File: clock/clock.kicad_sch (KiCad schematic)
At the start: 15 parts, among them Y1 Crystal_16MHz

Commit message: ch
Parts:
- removed C1, C2: C_0805_0.1uf, symbol Device:C
- removed C3, C4: C_0805_22pf, symbol Device:C
- removed D?: LED_0805, symbol Device:D
- removed J?: Conn_01x06, symbol Connector_Generic:Conn_01x06
- removed R1: R_0805_10k, symbol Device:R
- removed R?: R_0805_2.2k, symbol Device:R
- removed SW?: SW_SPST, symbol Switch:SW_SPST
- removed U?: ATmega328-P, Package_DIP:DIP-28_W7.62mm, symbol MCU_Microchip_ATmega:ATmega328-P
- removed Y1: Crystal_16MHz, symbol Device:Crystal
- added C1, C2, C5: C_0805_0.1uf, footprints:C_0805_2012Metric, symbol HPS:C_0805_0.1uf
- added C3, C4: C_0805_22pf, footprints:C_0805_2012Metric, symbol HPS:C_0805_22pf
- added D1: LED_0805, footprints:LED_0805_2012Metric, symbol HPS:LED_0805
- added J1: Conn_01x06, footprints:PinHeader_1x06_P2.54mm_Vertical, symbol HPS:Conn_01x06
- added R1: R_0805_10K, footprints:R_0805_2012Metric, symbol HPS:R_0805_10K
- added R2, R3: R_0805_47, footprints:R_0805_2012Metric, symbol HPS:R_0805_47
- added R4: R_0805_2.2K, footprints:R_0805_2012Metric, symbol HPS:R_0805_2.2K
- added SW1: Omron_B3F_SPST, footprints:SW_SPST_Omron_B3FS-100xP, symbol HPS:Omron_B3F_SPST
- added U1: ATmega328-PU, footprints:DIP-28_W7.62mm, symbol HPS:ATmega328-PU
- added Y1: Crystal_16MHz, footprints:Crystal_SMD_HC49-SD, symbol HPS:Crystal_16MHz
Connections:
- net GND: now also C1.2, C2.2, C3.2, C4.2, J1.5 (Pin_5), J1.6 (Pin_6), R4.2, SW1.1 (A), SW1.2 (A), U1.22 (GND), U1.8 (GND)
- net LED_SCK: now also D1.2 (A), U1.19 (PB5)
- net RESET: now also C5.1, R1.2, SW1.3 (B), SW1.4 (B), U1.1 (~{RESET}/PC6)
- net RXD: now also R3.2, U1.2 (PD0)
- net TXD: now also R2.2, U1.3 (PD1)
- net VCC: now also C2.1, R1.1, U1.20 (AVCC), U1.7 (VCC)
- new net: D1.1 (K), R4.1
- new net: J1.2 (Pin_2), R2.1
- new net: C3.1, U1.10 (XTAL2/PB7), Y1.1
- new net: C1.1, U1.21 (AREF)
- new net: C4.1, U1.9 (XTAL1/PB6), Y1.2
- new net: C5.2, J1.1 (Pin_1)
- new net: J1.3 (Pin_3), R3.1
- no-connect marks 0 -> 1

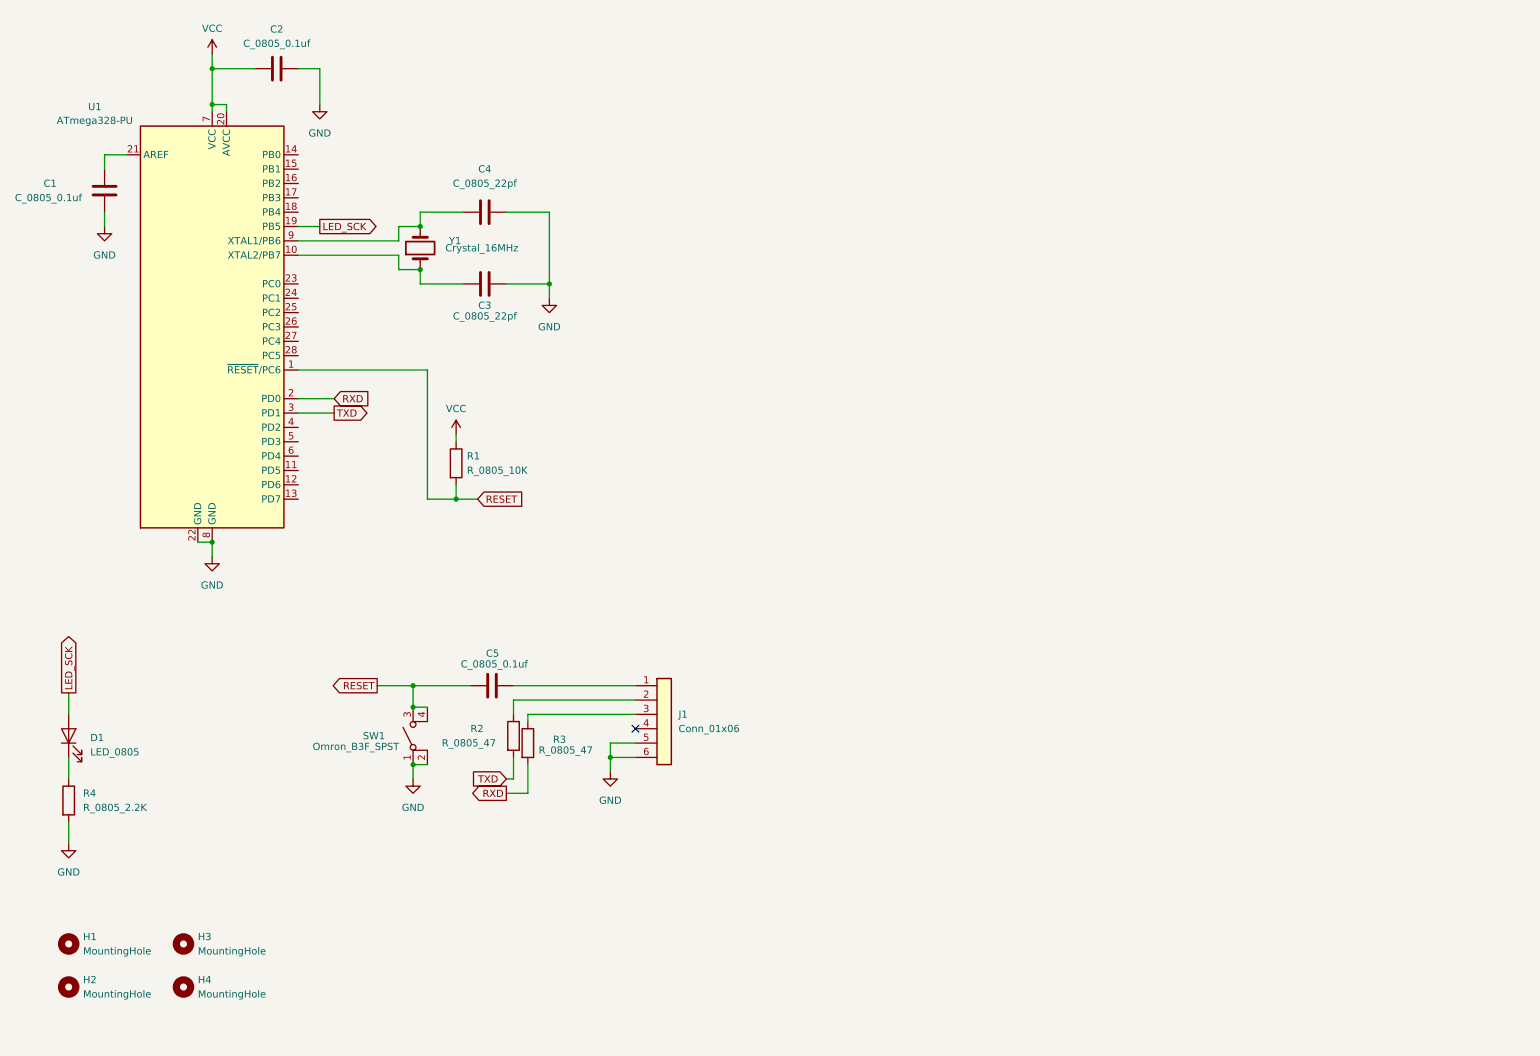
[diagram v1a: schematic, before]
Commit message: appending the clock
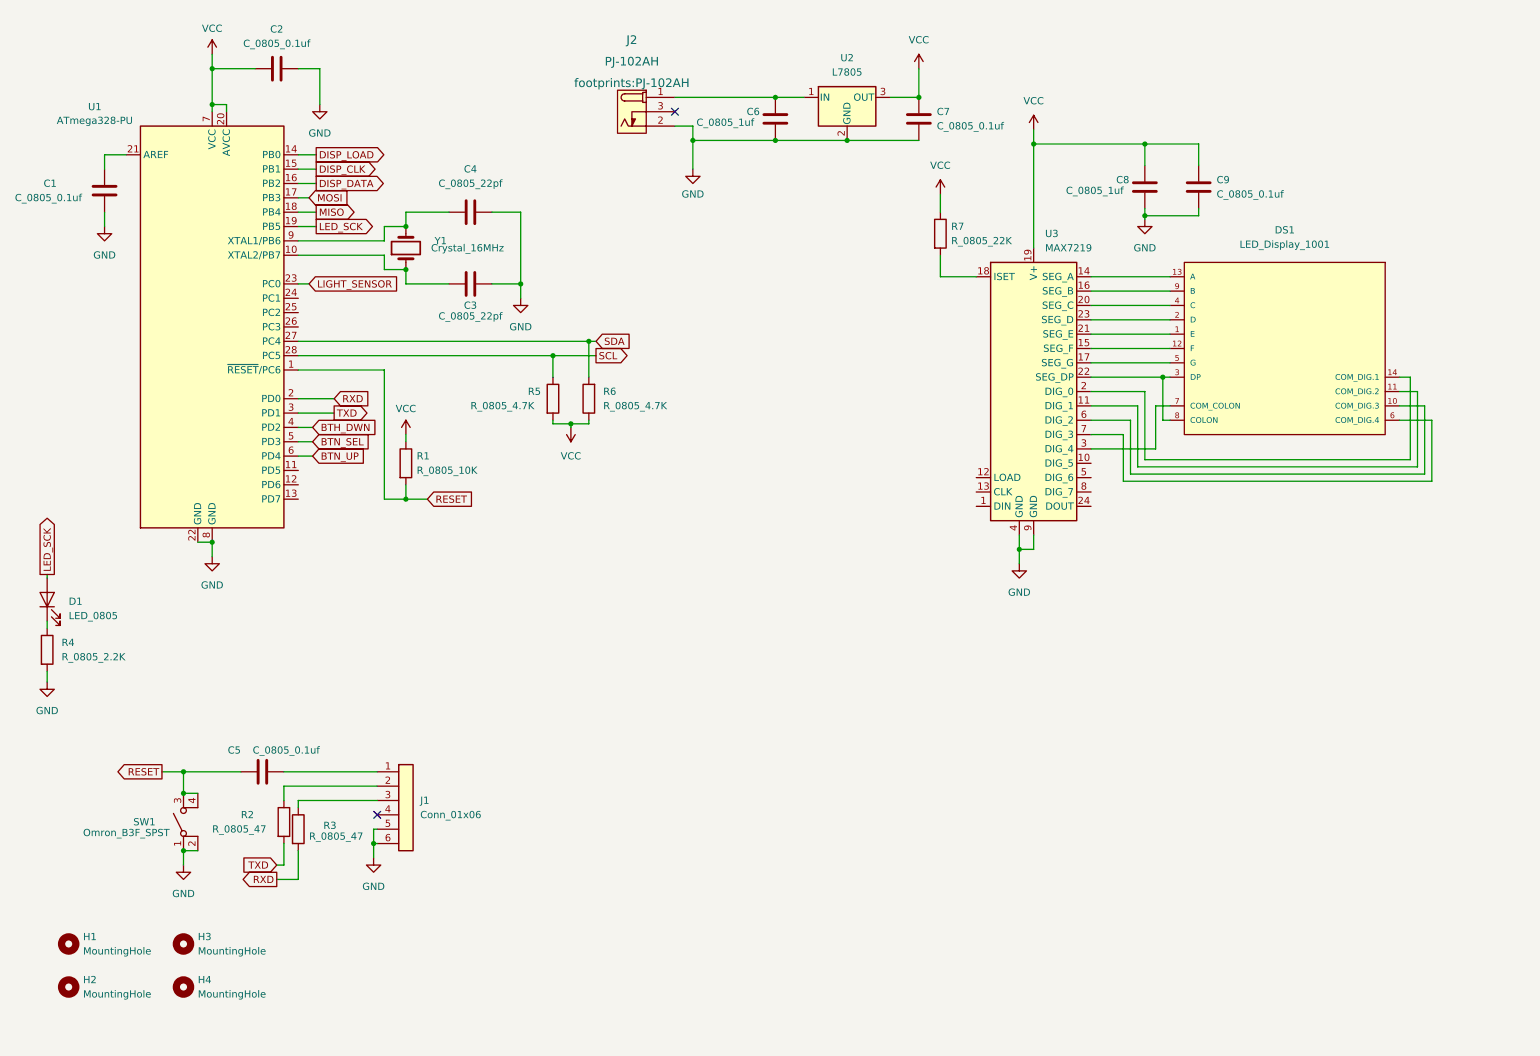
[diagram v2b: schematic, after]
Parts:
- added C6, C8: C_0805_1uf, footprints:C_0805_2012Metric, symbol HPS:C_0805_1uf
- added C7, C9: C_0805_0.1uf, footprints:C_0805_2012Metric, symbol HPS:C_0805_0.1uf
- added DS1: LED_Display_1001, footprints:Adafruit-1001-0-0-MFG, symbol HPS:LED_Display_1001
- added J2: PJ-102AH, footprints:PJ-102AH, symbol HPS:PJ-102AH
- added R5, R6: R_0805_4.7K, footprints:R_0805_2012Metric, symbol HPS:R_0805_4.7K
- added R7: R_0805_22K, footprints:R_0805_2012Metric, symbol HPS:R_0805_22K
- added U2: L7805, symbol HPS:L7805
- added U3: MAX7219, footprints:DIP-24_W7.62mm, symbol HPS:MAX7219
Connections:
- net GND: now also C6.2, C7.2, C8.2, C9.2, J2.2 (OUT), U2.2 (GND), U3.4 (GND), U3.9 (GND)
- net VCC: now also C7.1, C8.1, C9.1, R5.2, R6.1, R7.1, U2.3 (OUT), U3.19 (V+)
- net DISP_LOAD: now reaches U1.14 (PB0)
- net DISP_CLK: now reaches U1.15 (PB1)
- net DISP_DATA: now reaches U1.16 (PB2)
- net MOSI: now reaches U1.17 (PB3)
- net MISO: now reaches U1.18 (PB4)
- net LIGHT_SENSOR: now reaches U1.23 (PC0)
- net SDA: now reaches U1.27 (PC4)
- net SDA: now also R6.2
- net SCL: now reaches U1.28 (PC5)
- net SCL: now also R5.1
- net BTH_DWN: now reaches U1.4 (PD2)
- net BTN_SEL: now reaches U1.5 (PD3)
- net BTN_UP: now reaches U1.6 (PD4)
- new net: DS1.11 (COM_DIG.2), U3.11 (DIG_1)
- new net: DS1.13 (A), U3.14 (SEG_A)
- new net: DS1.12 (F), U3.15 (SEG_F)
- new net: DS1.9 (B), U3.16 (SEG_B)
- new net: DS1.5 (G), U3.17 (SEG_G)
- new net: R7.2, U3.18 (ISET)
- new net: DS1.14 (COM_DIG.1), U3.2 (DIG_0)
- new net: DS1.4 (C), U3.20 (SEG_C)
- new net: DS1.1 (E), U3.21 (SEG_E)
- new net: DS1.3 (DP), DS1.8 (COLON), U3.22 (SEG_DP)
- new net: DS1.2 (D), U3.23 (SEG_D)
- new net: DS1.7 (COM_COLON), U3.3 (DIG_4)
- new net: DS1.10 (COM_DIG.3), U3.6 (DIG_2)
- new net: DS1.6 (COM_DIG.4), U3.7 (DIG_3)
- new net: C6.1, J2.1 (POLE), U2.1 (IN)
- no-connect marks 1 -> 2
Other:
- moved on the sheet: C3, C4, C5, D1, J1, R1, R2, R3, R4, SW1, Y1

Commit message: pre review schematic
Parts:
- added BT1: Battery_Cell, footprints:BatteryHolder_Keystone_106_1x20mm, symbol HPS:Battery_Cell
- added J3: Conn_02x03_Odd_Even, footprints:PinHeader_2x03_P2.54mm_Vertical, symbol HPS:Conn_02x03_Odd_Even
- added R10, R11, R12: R_0805_10K, footprints:R_0805_2012Metric, symbol HPS:R_0805_10K
- added R8: PhotoconductivePhotocell, footprints:R_LDR_4.9x4.2mm_P2.54mm_Vertical, symbol HPS:PhotoconductivePhotocell
- added R9: R_0805_100K, footprints:R_0805_2012Metric, symbol HPS:R_0805_100K
- added SW2, SW3, SW4: Omron_B3F_SPST, footprints:SW_SPST_Omron_B3FS-100xP, symbol HPS:Omron_B3F_SPST
- added U4: DS1307_DIP-8, footprints:DIP-8_W7.62mm, symbol HPS:DS1307_DIP-8
- added Y2: Crystal_32768Hz, footprints:Crystal_SMD_2Pin_3.2x1.5mm, symbol HPS:Crystal_32768Hz
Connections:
- net SDA is gone; now on net SCL: R6.2, U1.27 (PC4)
- net BTN_SEL: now also R11.2, SW3.3 (B), SW3.4 (B)
- net BTN_UP: now also R10.2, SW2.3 (B), SW2.4 (B)
- net GND: now also BT1.2 (-), J3.6 (Pin_6), R9.2, SW2.1 (A), SW2.2 (A), SW3.1 (A), SW3.2 (A), SW4.1 (A), SW4.2 (A), U4.4 (GND)
- net LED_SCK: now also J3.5 (Pin_5)
- net LIGHT_SENSOR: now also R8.2, R9.1
- net MISO: now also J3.1 (Pin_1)
- net MOSI: now also J3.4 (Pin_4)
- net RESET: now also J3.3 (Pin_3)
- net SCL: now also U4.5 (SDA), U4.6 (SCL)
- net VCC: now also J3.2 (Pin_2), R10.1, R11.1, R12.1, R8.1, U4.8 (VCC)
- new net: U4.1 (X1), Y2.1
- new net: U4.2 (X2), Y2.2
- new net: BT1.1 (+), U4.3 (VBAT)
- new net BTN_DWN: R12.2, SW4.3 (B), SW4.4 (B)
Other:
- moved on the sheet: C1, C2, C3, C4, C5, C6, C7, C8, C9, D1, DS1, J1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

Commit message: lil changes
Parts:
- U2: footprint (none) -> footprints:TO-252-2
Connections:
- net DISP_CLK: now also U3.13 (CLK)
- net DISP_DATA: now also U3.1 (DIN)
- net DISP_LOAD: now also U3.12 (LOAD)
- net GND: now also J1.1 (Pin_1), J1.2 (Pin_2); no longer J1.5 (Pin_5), J1.6 (Pin_6)
- net LED_SCK: now also J3.3 (Pin_3); no longer J3.5 (Pin_5)
- net RESET: now also J3.5 (Pin_5); no longer J3.3 (Pin_3)
- net RXD: now also R2.2; no longer R3.2
- net TXD: now also R3.2; no longer R2.2
- net at R2.1: now also J1.5 (Pin_5); no longer J1.2 (Pin_2)
- net at C5.2: now also J1.6 (Pin_6); no longer J1.1 (Pin_1)
- net at J1.3 (Pin_3): no longer R3.1
- net at J1.4 (Pin_4): now also R3.1
- no-connect marks 2 -> 8

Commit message: ewwww
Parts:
- removed J2: PJ-102AH, footprints:PJ-102AH, symbol HPS:PJ-102AH
- added J2: Power_inlet_vertical, footprints:Wurth-694106402002, symbol HPS:Power_inlet_vertical
- added J4, J5: Conn_01x03, footprints:PinHeader_1x03_P2.54mm_Vertical, symbol HPS:Conn_01x03
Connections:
- net GND: now also J2.2 (OUT)
- net DEBUG_1: now reaches U1.11 (PD5)
- net DEBUG_1: now also J5.1 (Pin_1)
- net DEBUG_2: now reaches U1.12 (PD6)
- net DEBUG_2: now also J5.2 (Pin_2)
- net DEBUG_3: now reaches U1.13 (PD7)
- net DEBUG_3: now also J5.3 (Pin_3)
- net DEBUG_4: now reaches U1.24 (PC1)
- net DEBUG_4: now also J4.1 (Pin_1)
- net DEBUG_5: now reaches U1.25 (PC2)
- net DEBUG_5: now also J4.2 (Pin_2)
- net DEBUG_6: now reaches U1.26 (PC3)
- net DEBUG_6: now also J4.3 (Pin_3)
- net at C6.1, U2.1 (IN): now also J2.1 (POLE)

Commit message: did a copper pour
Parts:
- removed J4, J5: Conn_01x03, footprints:PinHeader_1x03_P2.54mm_Vertical, symbol HPS:Conn_01x03
- added J4, J5: Conn_01x05, footprints:PinHeader_1x05_P2.54mm_Vertical, symbol HPS:Conn_01x05
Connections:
- net DEBUG_1: now also J5.2 (Pin_2)
- net DEBUG_2: now also J5.3 (Pin_3)
- net DEBUG_3: now also J5.4 (Pin_4)
- net DEBUG_4: now also J4.2 (Pin_2)
- net DEBUG_5: now also J4.3 (Pin_3)
- net DEBUG_6: now also J4.4 (Pin_4)
- net GND: now also J4.5 (Pin_5), J5.5 (Pin_5)
- net VCC: now also J4.1 (Pin_1), J5.1 (Pin_1)
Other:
- moved on the sheet: C6, C7, D1, H1, H2, H3, H4, J2, J3, R4, R8, R9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

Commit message: adjusted a lil schemaric
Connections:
- net SCL: no longer R6.2, U1.27 (PC4), U4.5 (SDA)
- new net SDA: R6.2, U1.27 (PC4), U4.5 (SDA)
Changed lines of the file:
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@@
   (junction (at 205.74 127) (diameter 0) (color 0 0 0 0)
   )
-  (junction (at 89.535 85.09) (diameter 0) (color 0 0 0 0)
-  )
   (junction (at 71.12 110.49) (diameter 0) (color 0 0 0 0)
   )
@@
   (junction (at 133.35 20.32) (diameter 0) (color 0 0 0 0)
   )
+  (junction (at 91.44 72.39) (diameter 0) (color 0 0 0 0)
+  )
+  (junction (at 234.315 128.27) (diameter 0) (color 0 0 0 0)
+  )
+  (junction (at 261.62 141.605) (diameter 0) (color 0 0 0 0)
+  )
+  (junction (at 167.005 33.02) (diameter 0) (color 0 0 0 0)
+  )
+  (junction (at 71.12 62.23) (diameter 0) (color 0 0 0 0)
+  )
+  (junction (at 144.78 101.6) (diameter 0) (color 0 0 0 0)
+  )
+  (junction (at 133.35 24.13) (diameter 0) (color 0 0 0 0)
+  )
+  (junction (at 234.315 127) (diameter 0) (color 0 0 0 0)
+  )
+  (junction (at 159.385 67.945) (diameter 0) (color 0 0 0 0)
+  )
+  (junction (at 36.83 40.64) (diameter 0) (color 0 0 0 0)
+  )
+  (junction (at 132.715 179.705) (diameter 0) (color 0 0 0 0)
+  )
+  (junction (at 205.74 128.27) (diameter 0) (color 0 0 0 0)
+  )
+  (junction (at 36.83 118.11) (diameter 0) (color 0 0 0 0)
+  )
+  (junction (at 132.715 182.245) (diameter 0) (color 0 0 0 0)
+  )
+  (junction (at 144.78 109.22) (diameter 0) (color 0 0 0 0)
+  )
+  (junction (at 157.48 109.22) (diameter 0) (color 0 0 0 0)
+  )
+  (junction (at 36.83 34.29) (diameter 0) (color 0 0 0 0)
+  )
+  (junction (at 130.175 109.22) (diameter 0) (color 0 0 0 0)
+  )
+  (junction (at 234.315 141.605) (diameter 0) (color 0 0 0 0)
+  )
+  (junction (at 208.28 93.345) (diameter 0) (color 0 0 0 0)
+  )
   (junction (at 89.535 82.55) (diameter 0) (color 0 0 0 0)
-  )
-  (junction (at 91.44 72.39) (diameter 0) (color 0 0 0 0)
-  )
-  (junction (at 234.315 128.27) (diameter 0) (color 0 0 0 0)
-  )
-  (junction (at 261.62 141.605) (diameter 0) (color 0 0 0 0)
-  )
-  (junction (at 167.005 33.02) (diameter 0) (color 0 0 0 0)
-  )
-  (junction (at 71.12 62.23) (diameter 0) (color 0 0 0 0)
-  )
-  (junction (at 144.78 101.6) (diameter 0) (color 0 0 0 0)
-  )
-  (junction (at 133.35 24.13) (diameter 0) (color 0 0 0 0)
-  )
-  (junction (at 234.315 127) (diameter 0) (color 0 0 0 0)
-  )
-  (junction (at 159.385 67.945) (diameter 0) (color 0 0 0 0)
-  )
-  (junction (at 36.83 40.64) (diameter 0) (color 0 0 0 0)
-  )
-  (junction (at 132.715 179.705) (diameter 0) (color 0 0 0 0)
-  )
-  (junction (at 205.74 128.27) (diameter 0) (color 0 0 0 0)
-  )
-  (junction (at 36.83 118.11) (diameter 0) (color 0 0 0 0)
-  )
-  (junction (at 132.715 182.245) (diameter 0) (color 0 0 0 0)
-  )
-  (junction (at 144.78 109.22) (diameter 0) (color 0 0 0 0)
-  )
-  (junction (at 157.48 109.22) (diameter 0) (color 0 0 0 0)
-  )
-  (junction (at 36.83 34.29) (diameter 0) (color 0 0 0 0)
-  )
-  (junction (at 130.175 109.22) (diameter 0) (color 0 0 0 0)
-  )
-  (junction (at 234.315 141.605) (diameter 0) (color 0 0 0 0)
-  )
-  (junction (at 208.28 93.345) (diameter 0) (color 0 0 0 0)
   )
   (junction (at 261.62 127) (diameter 0) (color 0 0 0 0)
@@
     (stroke (width 0) (type default) (color 0 0 0 0))
   )
+  (wire (pts (xy 89.535 82.55) (xy 95.25 82.55))
+    (stroke (width 0) (type default) (color 0 0 0 0))
+  )
   (wire (pts (xy 227.33 34.29) (xy 227.33 34.925))
     (stroke (width 0) (type default) (color 0 0 0 0))
@@
     (stroke (width 0) (type default) (color 0 0 0 0))
   )
+  (wire (pts (xy 89.535 82.55) (xy 89.535 88.9))
+    (stroke (width 0) (type default) (color 0 0 0 0))
+  )
   (wire (pts (xy 196.85 77.47) (xy 196.85 83.185))
     (stroke (width 0) (type default) (color 0 0 0 0))
@@
     (stroke (width 0) (type default) (color 0 0 0 0))
   )
-  (wire (pts (xy 89.535 82.55) (xy 89.535 85.09))
-    (stroke (width 0) (type default) (color 0 0 0 0))
-  )
   (wire (pts (xy 226.695 81.28) (xy 281.305 81.28))
     (stroke (width 0) (type default) (color 0 0 0 0))
@@
     (stroke (width 0) (type default) (color 0 0 0 0))
   )
-  (wire (pts (xy 89.535 85.09) (xy 89.535 88.9))
-    (stroke (width 0) (type default) (color 0 0 0 0))
-  )
   (polyline (pts (xy 187.96 43.815) (xy 187.96 14.605))
     (stroke (width 0) (type default) (color 0 0 0 0))
@@
     (stroke (width 0) (type default) (color 0 0 0 0))
   )
-  (wire (pts (xy 83.185 85.09) (xy 89.535 85.09))
-    (stroke (width 0) (type default) (color 0 0 0 0))
-  )
   (polyline (pts (xy 102.87 127.635) (xy 102.235 22.86))
     (stroke (width 0) (type default) (color 0 0 0 0))
@@
     (stroke (width 0) (type default) (color 0 0 0 0))
   )
-  (wire (pts (xy 89.535 85.09) (xy 95.25 85.09))
+  (wire (pts (xy 83.185 85.09) (xy 95.25 85.09))
     (stroke (width 0) (type default) (color 0 0 0 0))
   )
@@
     (stroke (width 0) (type default) (color 0 0 0 0))
   )
-  (wire (pts (xy 89.535 82.55) (xy 95.25 82.55))
+  (wire (pts (xy 52.07 82.55) (xy 89.535 82.55))
     (stroke (width 0) (type default) (color 0 0 0 0))
   )
@@
     (stroke (width 0) (type default) (color 0 0 0 0))
   )
-  (wire (pts (xy 52.07 82.55) (xy 89.535 82.55))
-    (stroke (width 0) (type default) (color 0 0 0 0))
-  )
